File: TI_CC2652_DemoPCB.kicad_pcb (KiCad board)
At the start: 2 copper layers, 93.7 x 72.6 mm, 22 parts, among them J1 Conn_02x10_Odd_Even, J2 Conn_02x10_Odd_Even, J3 JpLedDIO6, J4 JpLedDIO7, J5 RX, J6 TX, J7 UART, J8 Conn_01x02, J9 Conn_ARM_JTAG_SWD_20, SW1 Reset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

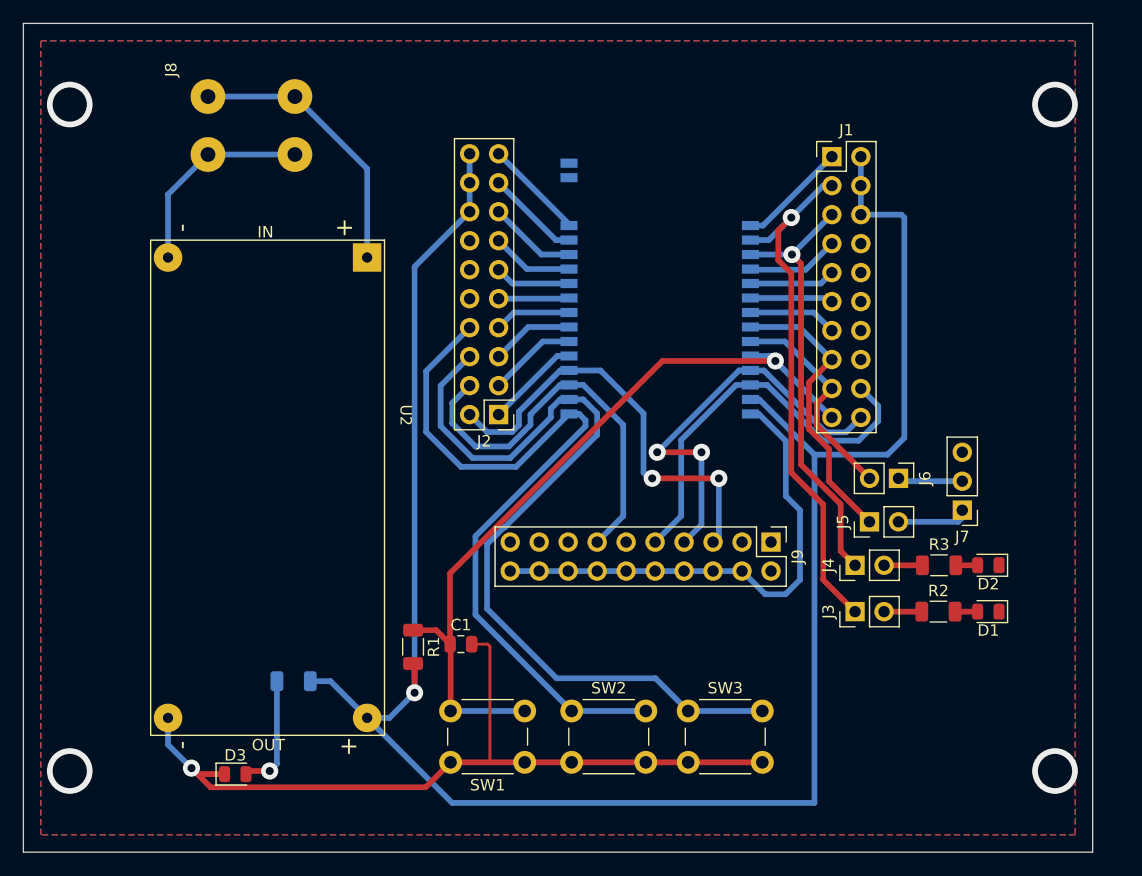
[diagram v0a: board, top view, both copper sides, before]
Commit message: сс2652 module moved to top side
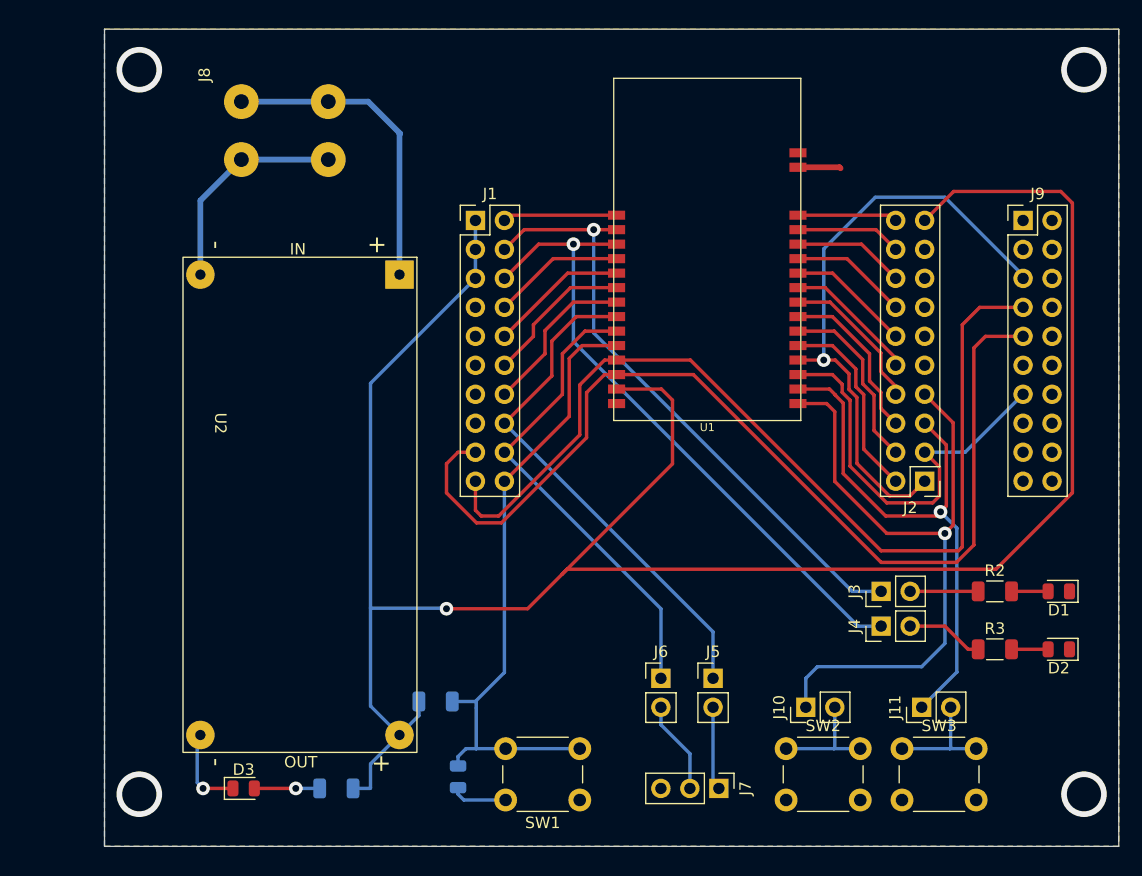
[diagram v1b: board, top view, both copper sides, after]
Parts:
- added J10: JpSWDIO14, Connector_PinHeader_2.54mm:PinHeader_1x02_P2.54mm_Vertical, F.Cu at (163.6, 116.3)
- added J11: JpSWDIO15, Connector_PinHeader_2.54mm:PinHeader_1x02_P2.54mm_Vertical, F.Cu at (173.7, 116.3)
- C1, R1: moved to B.Cu
- SW2: value BSL -> SW2
- SW3: value BSL -> SW3
- U1: moved to F.Cu
- moved J2 37.8 mm to (174.0, 96.5)
- moved J9 35.8 mm to (182.6, 73.7), turned to 0 degrees
- moved J7 32.4 mm to (156.0, 123.4), turned to -90 degrees
- moved J1 31.7 mm to (134.6, 73.7)
- moved J6 27.2 mm to (150.9, 113.8), turned to 0 degrees
- moved J5 19.4 mm to (155.4, 113.8), turned to 0 degrees
- moved SW2 19.1 mm to (161.8, 120.0)
- moved SW3 19.0 mm to (172.0, 120.0)
- moved C1 11.6 mm to (133.1, 122.4), turned to -90 degrees
- moved R4 10.1 mm to (122.4, 123.4)
- moved D2 9.61 mm to (185.8, 111.3)
- moved R3 8.84 mm to (180.1, 111.3)
- moved D1 6.43 mm to (185.8, 106.2)
- moved SW1 5.85 mm to (143.8, 124.5)
- moved J4 5.80 mm to (170.2, 109.2)
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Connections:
- J1 pad 1: /DIO_5 -> +3V3
- J1 pad 10: GND -> /DIO_9
- J1 pad 11: /DIO_10 -> GND
- J1 pad 12: GND -> /DIO_10
- J1 pad 13: /DIO_11 -> GND
- J1 pad 14: GND -> /DIO_11
- J1 pad 15: /DIO_12 -> GND
- J1 pad 16: GND -> /DIO_12
- J1 pad 17: /DIO_13 -> /JTAG_TCKC
- J1 pad 18: /JTAG_TCKC -> /DIO_13
- J1 pad 19: /RESET_N -> /JTAG_TMSC
- J1 pad 2: +3V3 -> /DIO_5
- J1 pad 20: /JTAG_TMSC -> /RESET_N
- J1 pad 3: /DIO_6 -> +3V3
- J1 pad 4: +3V3 -> /DIO_6
- J1 pad 5: /DIO_7 -> +3V3
- J1 pad 6: +3V3 -> /DIO_7
- J1 pad 7: /DIO_8 -> GND
- J1 pad 8: GND -> /DIO_8
- J1 pad 9: /DIO_9 -> GND
- J2 pad 1: /DIO_18 -> /DIO_17
- J2 pad 10: GND -> /DIO_22
- J2 pad 11: /DIO_23 -> GND
- J2 pad 12: GND -> /DIO_23
- J2 pad 13: /DIO_24 -> GND
- J2 pad 14: GND -> /DIO_24
- J2 pad 15: /DIO_25 -> +3V3
- J2 pad 16: +3V3 -> /DIO_25
- J2 pad 17: /DIO_26 -> +3V3
- J2 pad 18: +3V3 -> /DIO_26
- J2 pad 19: /DIO_27 -> +3V3
- J2 pad 2: /DIO_17 -> /DIO_18
- J2 pad 20: +3V3 -> /DIO_27
- J2 pad 3: /DIO_19 -> /DIO_16
- J2 pad 4: /DIO_16 -> /DIO_19
- J2 pad 5: /DIO_20 -> /DIO_15
- J2 pad 6: /DIO_15 -> /DIO_20
- J2 pad 7: /DIO_21 -> /DIO_14
- J2 pad 8: /DIO_14 -> /DIO_21
- J2 pad 9: /DIO_22 -> GND
- J6 pad 1: /TX -> /DIO_13
- J6 pad 2: /DIO_13 -> /TX
- SW2 pad 1: /DIO_14 -> Net-(SW2-Pad1)
- SW3 pad 1: /DIO_15 -> Net-(SW3-Pad1)
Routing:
- net GND: track 115.4 -> 16.3 mm, vias 5 -> 1
- net /JTAG_TCKC: track 35.4 -> 90.0 mm
- net /JTAG_TMSC: track 36.0 -> 86.1 mm, vias 2 -> 0
- net /DIO_15: track 74.1 -> 48.7 mm, vias 0 -> 1
- net /DIO_13: track 19.2 -> 41.8 mm
- net /DIO_12: track 25.6 -> 45.4 mm
- net /DIO_7: track 38.1 -> 56.9 mm
- net /DIO_17: track 38.2 -> 53.0 mm, vias 2 -> 1
- net /RESET_N: track 67.9 -> 56.1 mm, vias 1 -> 0
- net +3V3: track 180.5 -> 191.0 mm
- net Net-(SW3-Pad1): track 0.00 -> 10.2 mm
- net Net-(SW2-Pad1): track 0.00 -> 10.2 mm
- net /DIO_18: track 8.38 -> 17.2 mm
- net /DIO_19: track 7.77 -> 16.0 mm
- net /DIO_20: track 7.24 -> 14.7 mm
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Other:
- board size 93.7 x 72.6 mm -> 88.9 x 71.6 mm
